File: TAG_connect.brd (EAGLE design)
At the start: 22.1 x 14.3 mm, 4 parts, among them J2 RJ11-6PTH

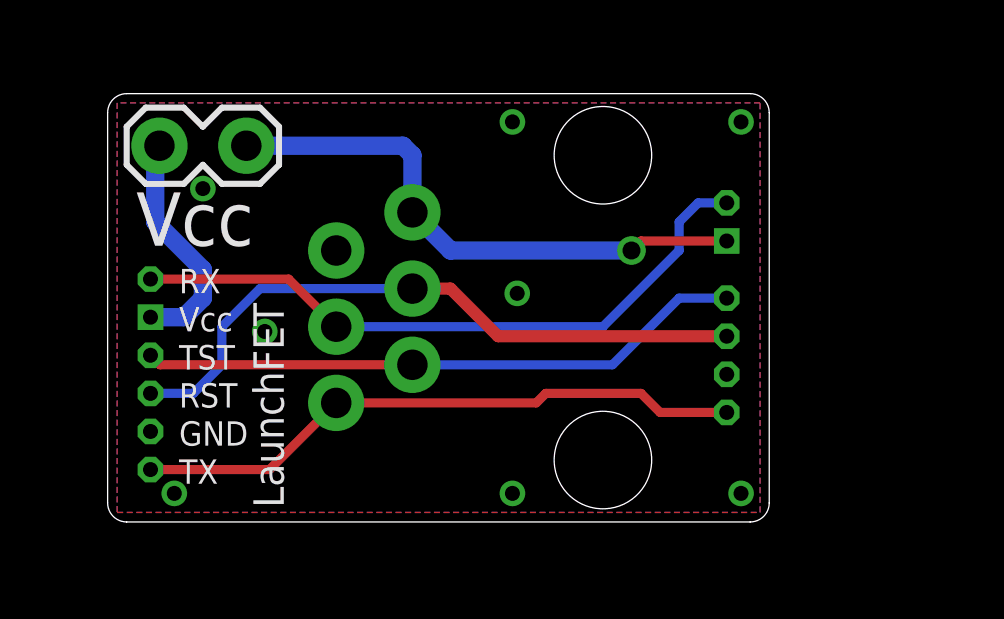
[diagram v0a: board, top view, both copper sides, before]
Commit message: new board, new pinout
Changed the pinout on the tag-connect cable to match new work
Added new SAFE-MSP adaptor board that uses a symmetric 2x10 .015" header
for programming.
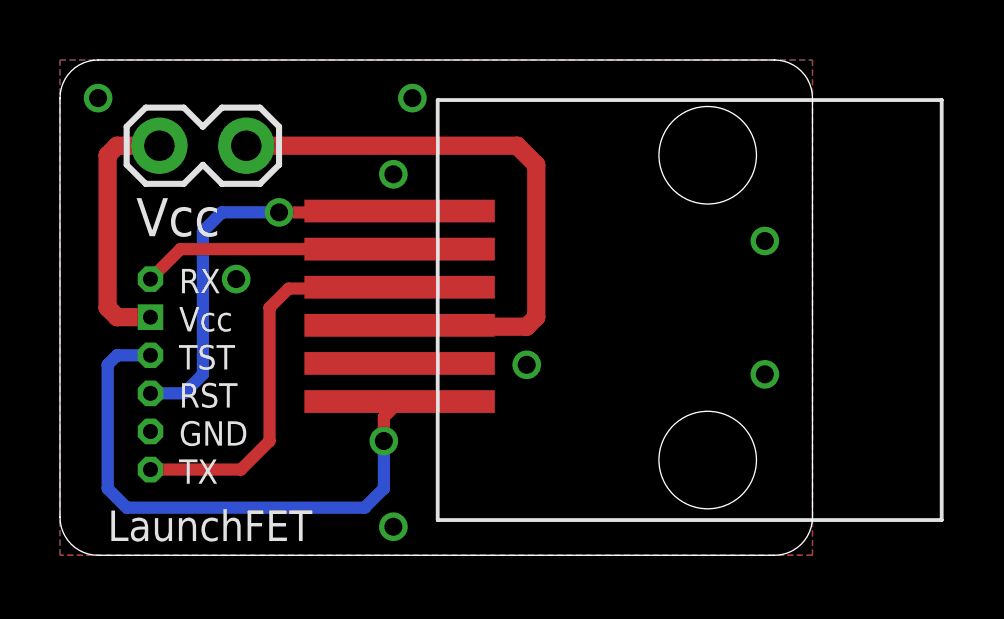
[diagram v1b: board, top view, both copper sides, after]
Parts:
- removed J2: RJ11-6PTH, SparkFun-Connectors:RJ11-6
- removed U$5: 6-PIN-ICSPSAFE-MSP, LaunchFET:SAFEMSP-6PIN
- added U$1: RJ-45SMD, LaunchFET:MOLEX_RJ45_SMD
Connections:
- removed net RESET: J2.4, U$4.RST, U$5.RST
- new net RST: U$1.RST, U$4.RST
- net GND: now also U$1.GND; no longer J2.5, U$5.GND
- net RX: now also U$1.RX; no longer J2.3, U$5.RX
- net TEST: now also U$1.TEST; no longer J2.2, U$5.TST
- net TX: now also U$1.TX; no longer J2.1, U$5.TX
- net VCC_TARGET: now also U$1.VCC; no longer J2.6, U$5.VCC
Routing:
- net RESET: track 22.1 -> 0.00 mm
- net RST: track 0.00 -> 13.6 mm, vias 0 -> 1
- net RX: track 22.1 -> 8.72 mm
- net TX: track 20.5 -> 13.4 mm
- net TEST: track 20.3 -> 18.5 mm, vias 0 -> 1
- net VCC_TARGET: track 18.7 -> 19.7 mm, vias 1 -> 0
- net VCC_FET: track 7.80 -> 8.50 mm
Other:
- board size 22.1 x 14.3 mm -> 25.1 x 16.5 mm
